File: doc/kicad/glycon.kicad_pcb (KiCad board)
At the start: 2 copper layers, 200 x 100 mm, 53 parts, among them J1 Arduino/system bus header, J2 PMOD USBUART conn, J3 Conn_01x02, J4 Conn_02x24_Odd_Even, Q1 IRF9540N, Q2 IRF9540N, SW1 SW_Push, SW2 SW_Push, U0 Z80CPU, U1 628128_DIP32_SSOP32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

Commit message: update gerber plot files
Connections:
- net /IEO1 renamed /IEI0
- net /IEO2 renamed /IEI1

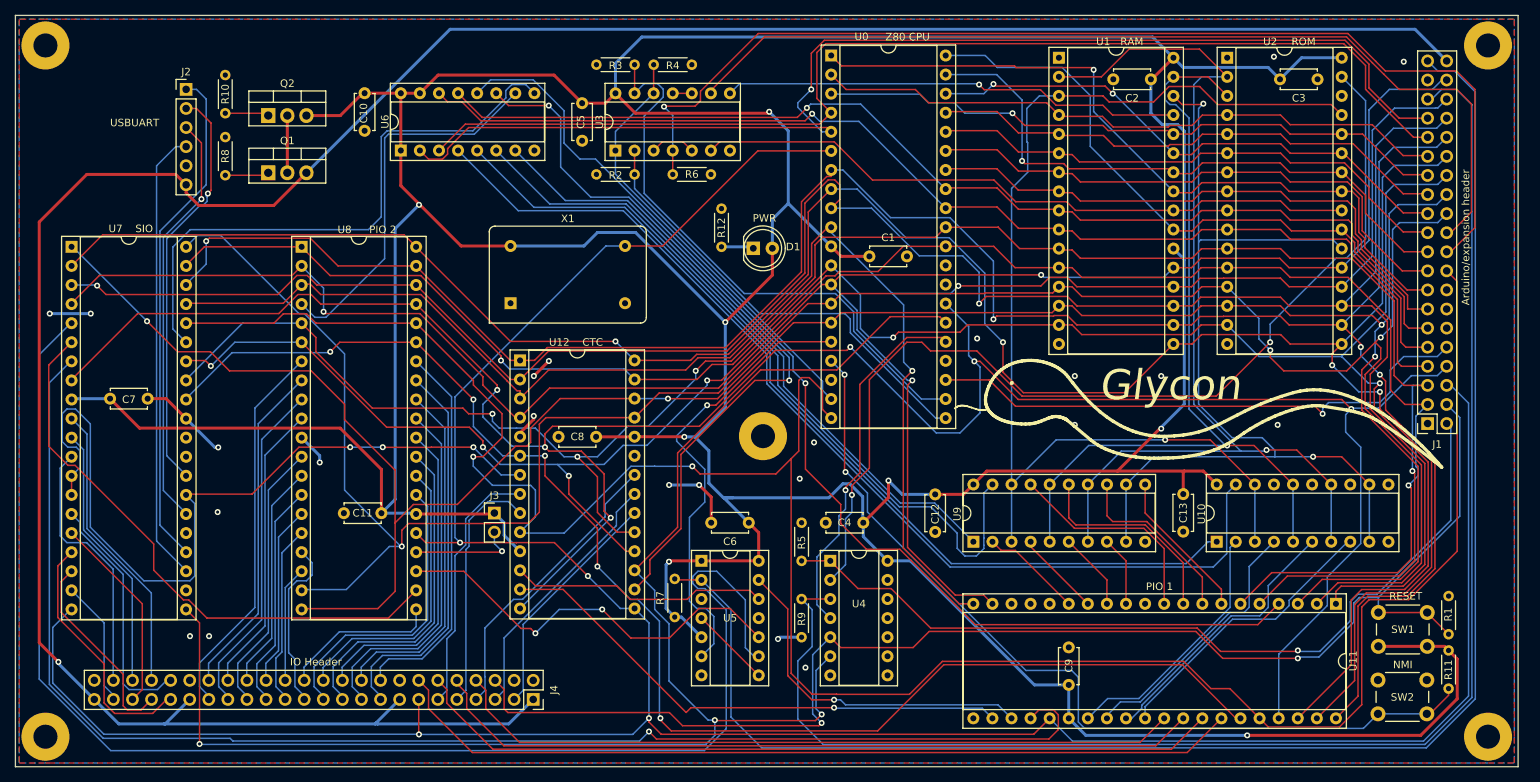
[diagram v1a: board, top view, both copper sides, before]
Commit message: update pinout schematic + add old revision of board under 'glycon_rev1.0'
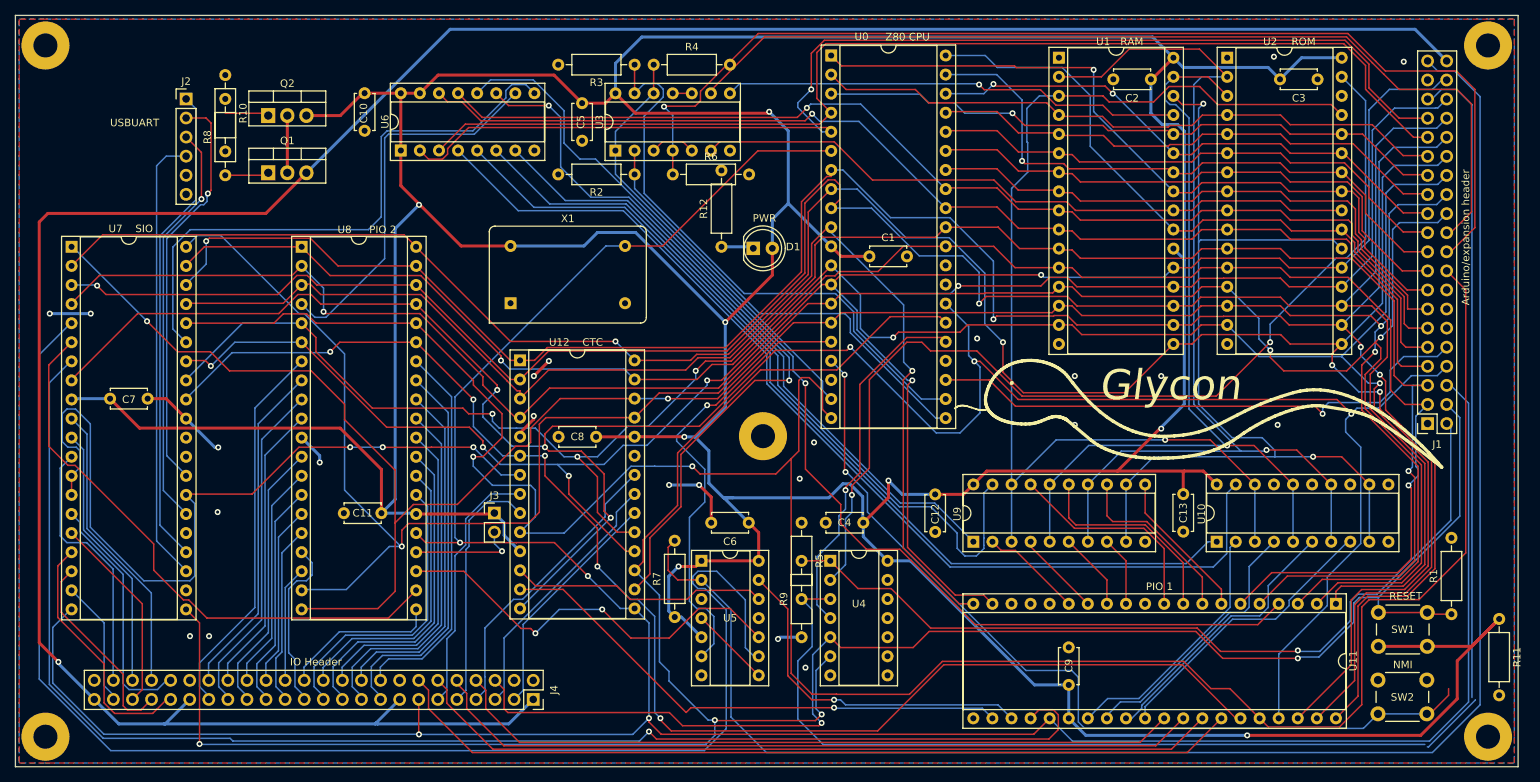
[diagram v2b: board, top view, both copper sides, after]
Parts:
- R1, R10, R11, R12, R2, R3, R4, R5, R6, R7, R9: footprint Resistor_THT:R_Axial_DIN0204_L3.6mm_D1.6mm_P5.08mm_Horizontal -> Resistor_THT:R_Axial_DIN0207_L6.3mm_D2.5mm_P10.16mm_Horizontal
- R8: value 1K -> 10K; footprint Resistor_THT:R_Axial_DIN0204_L3.6mm_D1.6mm_P5.08mm_Horizontal -> Resistor_THT:R_Axial_DIN0207_L6.3mm_D2.5mm_P10.16mm_Horizontal
- moved R11 7.93 mm to (221.0, 100.3)
- moved R1 2.69 mm to (214.6, 99.7)
- moved J2 1.27 mm to (46.2, 31.1)
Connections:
- J2 pad 6: +5V -> unconnected-(J2-Pin_6)
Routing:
- net VDD: track 733.6 -> 746.2 mm
- net (no net): track 0.00 -> 8.97 mm
- net /BUSRQ: track 201.1 -> 192.2 mm
- net /~{INTIN}: track 215.8 -> 223.3 mm
- net +5V: track 341.0 -> 337.0 mm
- net /RTSB: track 67.5 -> 64.3 mm
- net /~{IORQ}: track 312.9 -> 314.6 mm
- net /TxDB: track 55.6 -> 54.4 mm
- net /RESET: track 184.7 -> 184.0 mm
- net /RxDB: track 55.0 -> 54.4 mm
- net /CTSB: track 60.6 -> 60.1 mm

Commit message: minor schematic updates
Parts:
- added R13: 10K, Resistor_THT:R_Axial_DIN0207_L6.3mm_D2.5mm_P10.16mm_Horizontal, F.Cu at (243.8, 62.2)
- added R14: 10K, Resistor_THT:R_Axial_DIN0207_L6.3mm_D2.5mm_P10.16mm_Horizontal, F.Cu at (243.8, 58.2)
- added R15: 10K, Resistor_THT:R_Axial_DIN0207_L6.3mm_D2.5mm_P10.16mm_Horizontal, F.Cu at (243.8, 54.1)
- added R16: 10K, Resistor_THT:R_Axial_DIN0207_L6.3mm_D2.5mm_P10.16mm_Horizontal, F.Cu at (257.1, 54.1)
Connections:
- J1 pad 12: unconnected-(J1-Pin_12) -> /A17
- J1 pad 14: unconnected-(J1-Pin_14) -> /A16
- J1 pad 16: unconnected-(J1-Pin_16) -> /A15
- J1 pad 37: unconnected-(J1-Pin_37) -> /A14
- U1 pad 22: VDD -> Earth
- U6 pad 1: VDD -> Earth
- U6 pad 15: VDD -> Earth
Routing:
- net /BUSRQ: track 192.2 -> 86.2 mm
- net /ROM WE: track 113.3 -> 219.4 mm
- net VDD: track 746.2 -> 709.3 mm, vias 8 -> 7

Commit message: schematic fixes
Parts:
- added J5: USB_B, Connector_USB:USB_B_Lumberg_2411_02_Horizontal, F.Cu at (58.4, 35.6)
- added R17: 10K, Resistor_THT:R_Axial_DIN0207_L6.3mm_D2.5mm_P10.16mm_Horizontal, F.Cu at (245.7, 38.1)
- added R18: 10K, Resistor_THT:R_Axial_DIN0207_L6.3mm_D2.5mm_P10.16mm_Horizontal, F.Cu at (245.7, 42.1)
- U5: value 74LS21 -> 74LS08
- moved R8 40.7 mm to (11.4, 33.7)
- moved R10 31.8 mm to (20.3, 34.3)
- moved Q2 21.7 mm to (76.2, 43.8)
- moved Q1 6.97 mm to (63.5, 43.8)
- moved U5 0.77 mm to (115.6, 92.7)
- moved U4 0.17 mm to (132.1, 92.7)
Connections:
- R2 pad 1: /~{RD} -> /~{IORD}
- U0 pad 21: /~{RD} -> /~{IORD}
- U0 pad 24: unconnected-(U0-~{WAIT}) -> VDD
- U11 pad 16: Earth -> unconnected-(U11-~{ASTB})
- U11 pad 17: Earth -> unconnected-(U11-~{BSTB})
- U11 pad 18: Earth -> unconnected-(U11-ARDY)
- U11 pad 21: Earth -> unconnected-(U11-BRDY)
- U11 pad 37: /~{M1} -> Net-(U11-~{M1})
- U12 pad 12: Net-(U12-~{INT}) -> Net-(U11-~{INT})
- U3 pad 2: /~{RD} -> /~{IORD}
- U5 pad 1: VDD -> /~{INTIN}
- U5 pad 10: Net-(U8-~{INT}) -> /~{RESET}
- U5 pad 12: Net-(U12-~{INT}) -> (no net)
- U5 pad 13: Net-(U11-~{INT}) -> (no net)
- U5 pad 2: /~{INTIN} -> Net-(U11-~{INT})
- U5 pad 3: (no net) -> /~{INT}
- U5 pad 4: Net-(U5-Pad4) -> /~{RESET}
- U5 pad 5: VDD -> /~{M1}
- U5 pad 6: /~{INT} -> Net-(U11-~{M1})
- U5 pad 8: Net-(U5-Pad4) -> Net-(U8-~{M1})
- U5 pad 9: Net-(U7-~{INT}) -> /~{M1}
- U7 pad 5: Net-(U7-~{INT}) -> Net-(U11-~{INT})
- U8 pad 23: Net-(U8-~{INT}) -> Net-(U11-~{INT})
- U8 pad 37: /~{M1} -> Net-(U8-~{M1})
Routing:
- net /~{INTIN}: track 223.3 -> 0.00 mm
- net Net-(U7-~{INT}): track 185.9 -> 0.00 mm
- net /RAM/ROM OE: track 148.8 -> 3.18 mm, vias 1 -> 0
- net /RAM WE: track 127.1 -> 0.00 mm
- net /ROM WE: track 219.4 -> 109.3 mm
- net /BUSRQ: track 86.2 -> 0.00 mm
- net Net-(U11-~{M1}): track 0.00 -> 80.4 mm, vias 0 -> 1
- net VDD: track 709.3 -> 641.8 mm
- net /~{INT}: track 60.2 -> 0.00 mm, vias 1 -> 0
- net /~{IORD}: track 185.9 -> 246.0 mm
- net /~{RD}: track 60.2 -> 0.00 mm
- net Net-(U8-~{INT}): track 55.1 -> 0.00 mm, vias 2 -> 0
- net Net-(U11-~{INT}): track 46.5 -> 0.00 mm, vias 1 -> 0
- net /A15: track 113.7 -> 153.0 mm, vias 1 -> 2
- net Net-(U12-~{INT}): track 34.3 -> 0.00 mm
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
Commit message: More schematic fixes
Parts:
- removed R13, R14, R15, R16, R2, R3, R4, R6: 10K, Resistor_THT:R_Axial_DIN0207_L6.3mm_D2.5mm_P10.16mm_Horizontal
- added RN1: 10K, Resistor_THT:R_Array_SIP9, F.Cu at (80.0, 26.7)
- moved R18 213.8 mm to (32.4, 29.2)
- moved R17 213.1 mm to (33.0, 25.4)
- moved R8 24.2 mm to (33.7, 43.2)
- moved R10 8.98 mm to (29.2, 33.0)
- moved U5 0.64 mm to (114.9, 92.7)
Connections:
- net /~{IORD} renamed /~{RD}
- U11 pad 1: /D5 -> /D2
- U11 pad 19: /D7 -> /D0
- U11 pad 2: /D0 -> /D7
- U11 pad 20: /D6 -> /D1
- U11 pad 3: /D1 -> /D6
- U11 pad 37: Net-(U11-~{M1}) -> /PIO_~{M1}
- U11 pad 38: /D2 -> /D5
- U11 pad 39: /D3 -> /D4
- U11 pad 40: /D4 -> /D3
- U5 pad 4: /~{RESET} -> (no net)
- U5 pad 5: /~{M1} -> (no net)
- U5 pad 6: Net-(U11-~{M1}) -> (no net)
- U5 pad 8: Net-(U8-~{M1}) -> /PIO_~{M1}
- U8 pad 37: Net-(U8-~{M1}) -> /PIO_~{M1}
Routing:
- net Net-(U11-~{M1}): track 80.4 -> 0.00 mm, vias 1 -> 0
- net /PIO_~{M1}: track 0.00 -> 80.4 mm, vias 0 -> 1
- net /D5: track 299.7 -> 317.7 mm
- net /D2: track 277.8 -> 261.5 mm
- net /D6: track 262.4 -> 250.0 mm
- net /D7: track 280.8 -> 275.4 mm
- net /D1: track 310.7 -> 306.2 mm
- net /D4: track 296.6 -> 301.1 mm
- net /D0: track 308.2 -> 304.2 mm
- net /~{IORQ}: track 314.6 -> 315.7 mm
- net /D3: track 315.0 -> 314.2 mm
- removed copper zone on B.Cu, net Earth
- removed copper zone on F.Cu, net Earth
